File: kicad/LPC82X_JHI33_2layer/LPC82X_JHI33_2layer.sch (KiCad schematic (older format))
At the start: 27 parts, among them J1 Conn_02x09_Odd_Even, J2 Conn_02x09_Odd_Even, J3 JTAG_2X05, U1 LPC824M201JHI33, Y1 12MHz

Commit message: added bulk decoupling 0805 increased clearance of ground plane
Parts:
- added C7: 10u, SquantorRcl:C_0805, symbol Device:C
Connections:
- net VDD: now also C7.2
- net VSS: now also C7.1
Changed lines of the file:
@@
 EESchema Schematic File Version 4
-LIBS:LPC82X_JHI33-cache
 EELAYER 26 0
 EELAYER END
@@
 	1    0    0    -1
 $EndComp
+$Comp
+L Device:C C7
+U 1 1 5BD6A440
+P 2400 1700
+F 0 "C7" H 2515 1746 50  0000 L CNN
+F 1 "10u" H 2515 1655 50  0000 L CNN
+F 2 "SquantorRcl:C_0805" H 2438 1550 50  0001 C CNN
+F 3 "~" H 2400 1700 50  0001 C CNN
+	1    2400 1700
+	1    0    0    -1
+$EndComp
+$Comp
+L power:VSS #PWR0125
+U 1 1 5BD6A894
+P 2400 1500
+F 0 "#PWR0125" H 2400 1350 50  0001 C CNN
+F 1 "VSS" V 2417 1628 50  0000 L CNN
+F 2 "" H 2400 1500 50  0001 C CNN
+F 3 "" H 2400 1500 50  0001 C CNN
+	1    2400 1500
+	1    0    0    -1
+$EndComp
+$Comp
+L power:VDD #PWR0126
+U 1 1 5BD6A935
+P 2400 1900
+F 0 "#PWR0126" H 2400 1750 50  0001 C CNN
+F 1 "VDD" V 2417 2028 50  0000 L CNN
+F 2 "" H 2400 1900 50  0001 C CNN
+F 3 "" H 2400 1900 50  0001 C CNN
+	1    2400 1900
+	-1   0    0    1
+$EndComp
+Wire Wire Line
+	2400 1500 2400 1550
+Wire Wire Line
+	2400 1850 2400 1900
 $EndSCHEMATC

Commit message: silk screen updates
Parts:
- S1: value 2pin_tact_switch -> Reset
- S2: value 2pin_tact_switch -> Boot
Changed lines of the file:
@@
 EESchema Schematic File Version 4
+LIBS:LPC82X_JHI33_2layer-cache
 EELAYER 26 0
 EELAYER END
@@
 P 1850 4600
 F 0 "S1" H 1600 4700 60  0000 C CNN
-F 1 "2pin_tact_switch" H 1850 4831 60  0000 C CNN
+F 1 "Reset" H 1850 4831 60  0000 C CNN
 F 2 "SquantorButtons:TD-85XU" H 1850 4600 60  0001 C CNN
 F 3 "" H 1850 4600 60  0001 C CNN
@@
 P 1850 5100
 F 0 "S2" H 1600 5200 60  0000 C CNN
-F 1 "2pin_tact_switch" H 1850 5331 60  0000 C CNN
+F 1 "Boot" H 1850 5331 60  0000 C CNN
 F 2 "SquantorButtons:TD-85XU" H 1850 5100 60  0001 C CNN
 F 3 "" H 1850 5100 60  0001 C CNN

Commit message: updated versionnumber
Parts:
- N2: value 20181026 -> 20181028
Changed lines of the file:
@@
 P 850 7700
 F 0 "N2" H 850 7800 60  0000 C CNN
-F 1 "20181026" H 850 7700 60  0000 C CNN
+F 1 "20181028" H 850 7700 60  0000 C CNN
 F 2 "SquantorLabels:Label_version" H 850 7700 60  0001 C CNN
 F 3 "" H 850 7700 60  0001 C CNN

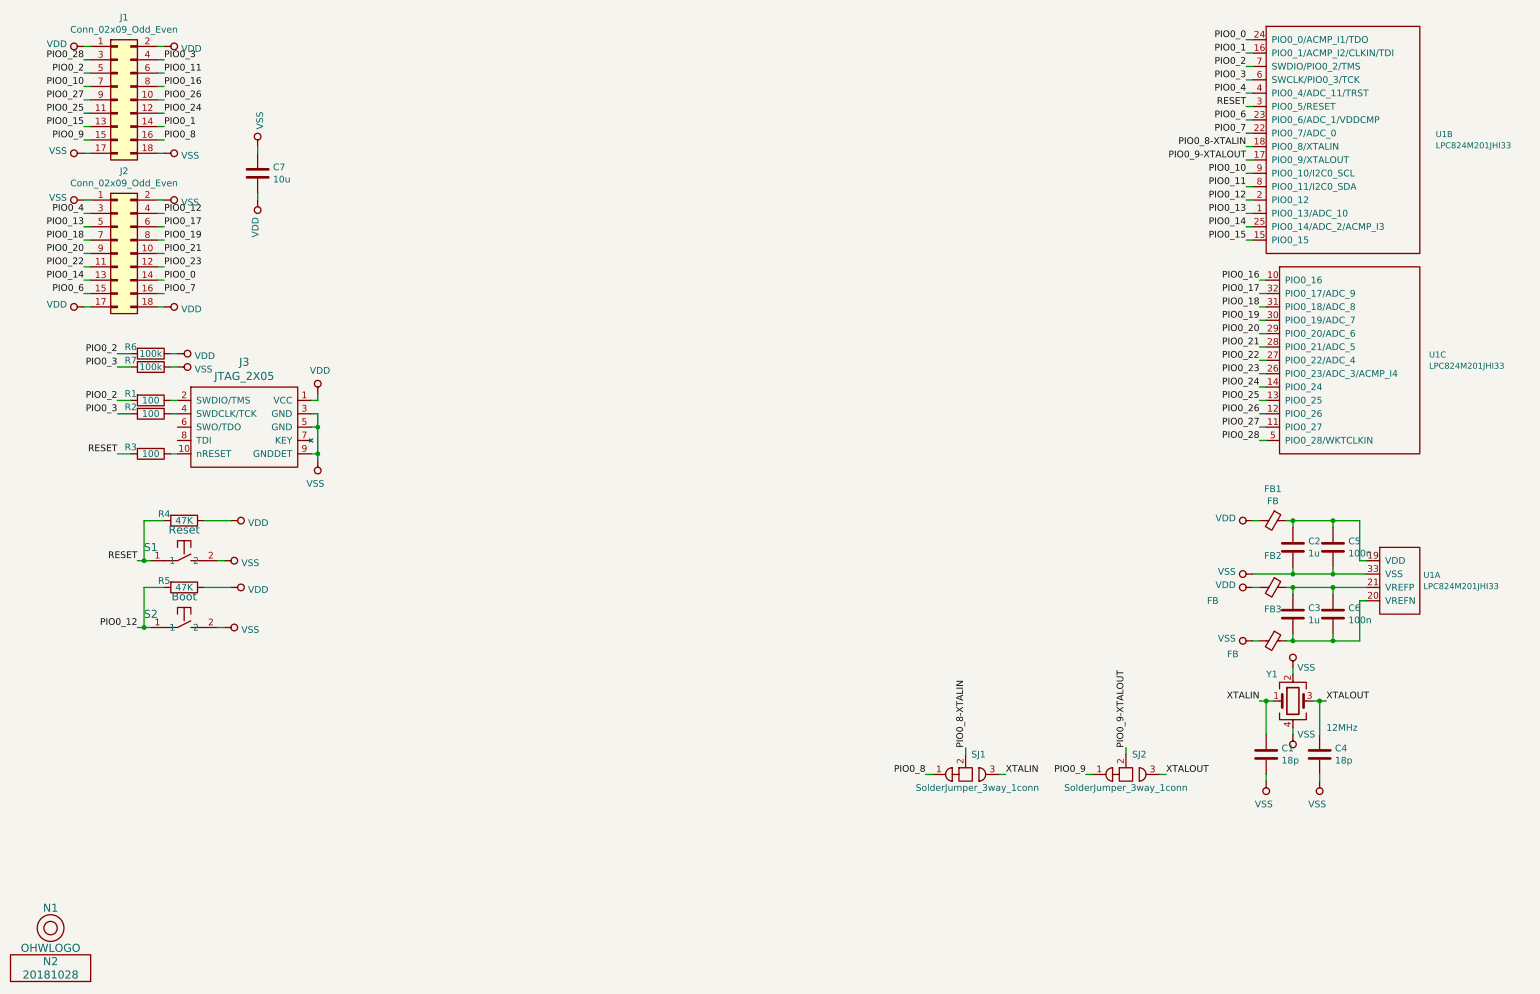
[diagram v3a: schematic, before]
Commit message: removed some parts from schematics to simplify the breakout
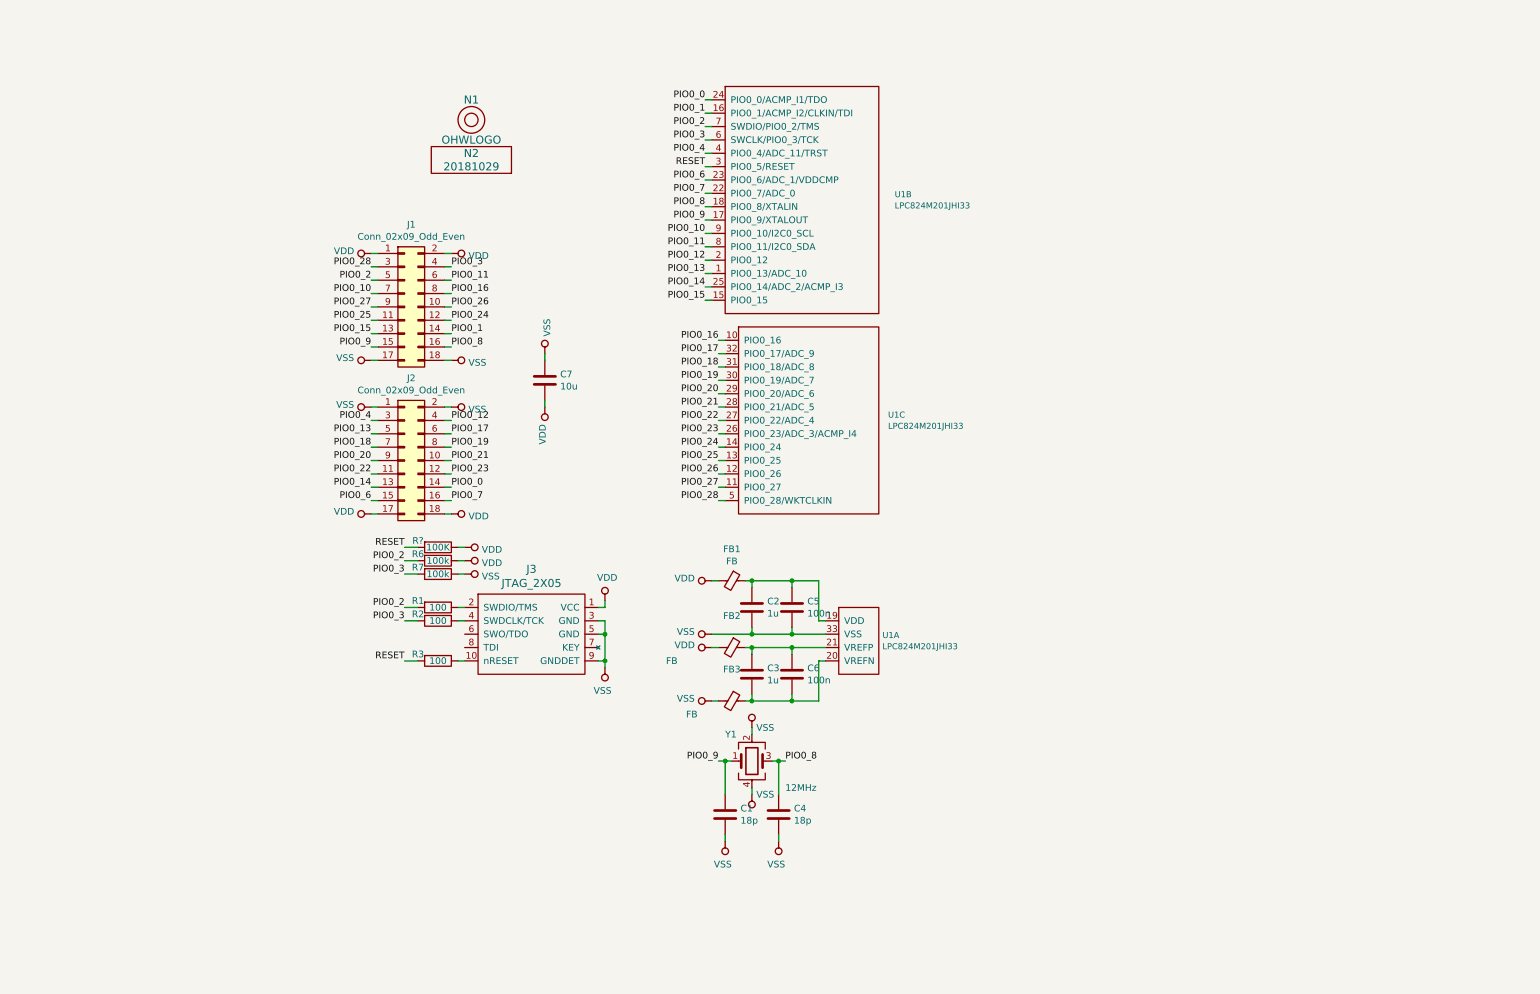
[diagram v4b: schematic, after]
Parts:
- removed R4, R5: 47K, SquantorRcl:R_0402_hand, symbol Device:R
- removed S1: Reset, SquantorButtons:TD-85XU, symbol SquantorButtons:2pin_tact_switch
- removed S2: Boot, SquantorButtons:TD-85XU, symbol SquantorButtons:2pin_tact_switch
- removed SJ1, SJ2: SolderJumper_3way_1conn, SquantorSpecial:solder_jumper_3way_12conn, symbol SquantorSpecial:SolderJumper_3way_1conn
- added R?: 100K, SquantorRcl:R_0402_hand, symbol Device:R
- N2: value 20181028 -> 20181029
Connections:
- net PIO0_8-XTALIN is gone; now on net PIO0_8: U1.18 (PIO0_8/XTALIN)
- net PIO0_9-XTALOUT is gone; now on net PIO0_9: U1.17 (PIO0_9/XTALOUT)
- net XTALIN is gone; now on net PIO0_9: C1.1, Y1.1
- net XTALOUT is gone; now on net PIO0_8: C4.1, Y1.3
- net RESET: now also R?.2
- net VDD: now also R?.1
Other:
- moved on the sheet: C1, C2, C3, C4, C5, C6, C7, FB1, FB2, FB3, J1, J2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

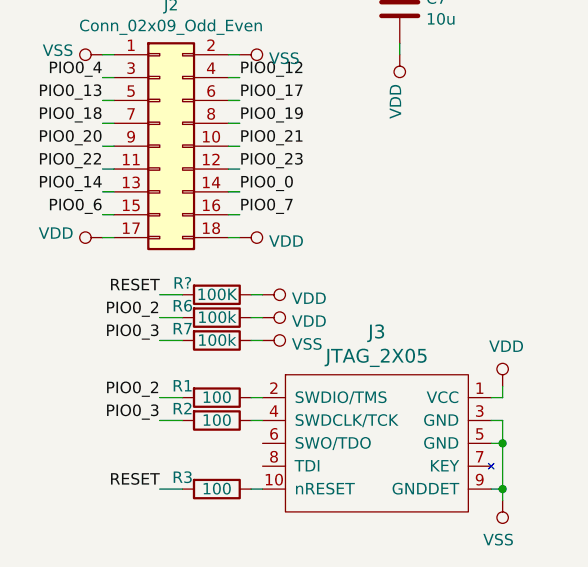
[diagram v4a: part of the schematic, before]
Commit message: updated schematic bits updated board and rerouted with some deletions, lets see if we can shrink the board a bit
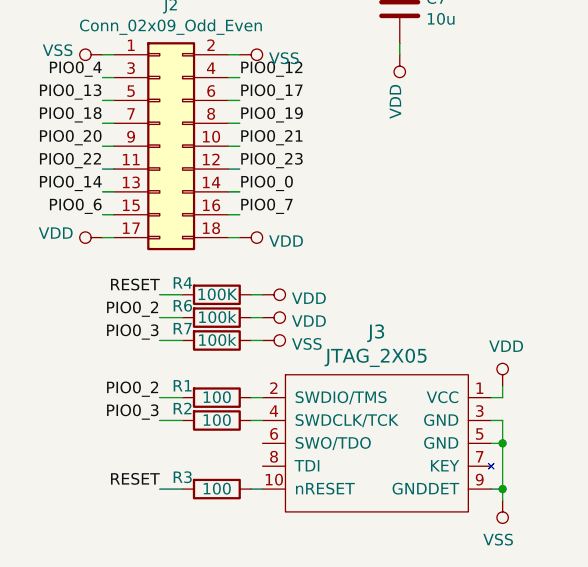
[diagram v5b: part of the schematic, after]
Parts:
- gave numbers to parts that had none: 1
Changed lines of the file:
@@
 PIO0_8
 $Comp
-L Device:R R?
+L Device:R R4
 U 1 1 5BD88002
 P 3750 4500
-F 0 "R?" V 3700 4350 50  0000 C CNN
+F 0 "R4" V 3700 4350 50  0000 C CNN
 F 1 "100K" V 3750 4500 50  0000 C CNN
 F 2 "SquantorRcl:R_0402_hand" V 3680 4500 50  0001 C CNN
@@
 RESET
 $Comp
-L power:VDD #PWR?
+L power:VDD #PWR0111
 U 1 1 5BD880D2
 P 3950 4500
-F 0 "#PWR?" H 3950 4350 50  0001 C CNN
+F 0 "#PWR0111" H 3950 4350 50  0001 C CNN
 F 1 "VDD" V 3967 4628 50  0000 L CNN
 F 2 "" H 3950 4500 50  0001 C CNN

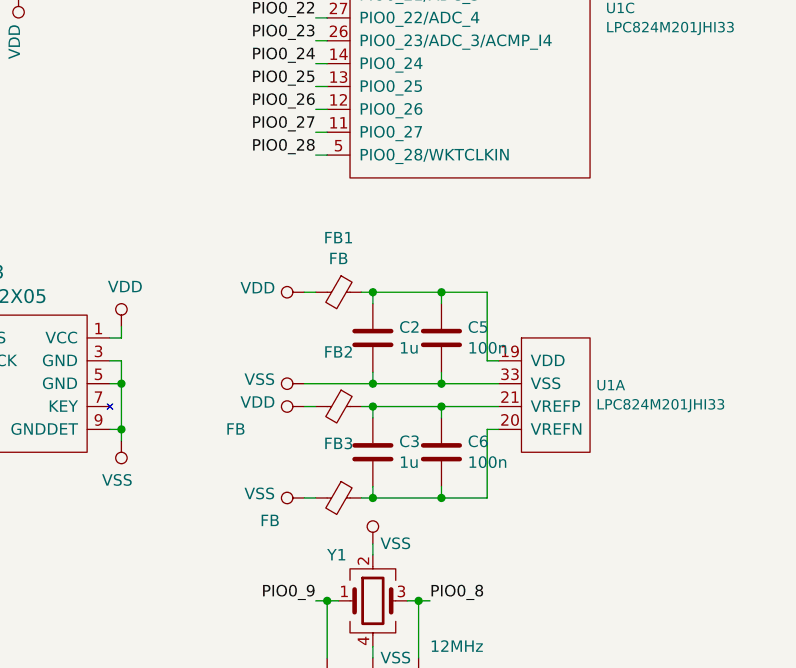
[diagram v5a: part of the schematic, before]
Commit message: updated schematic, added VDD jumper, added top groundplane, completed layout
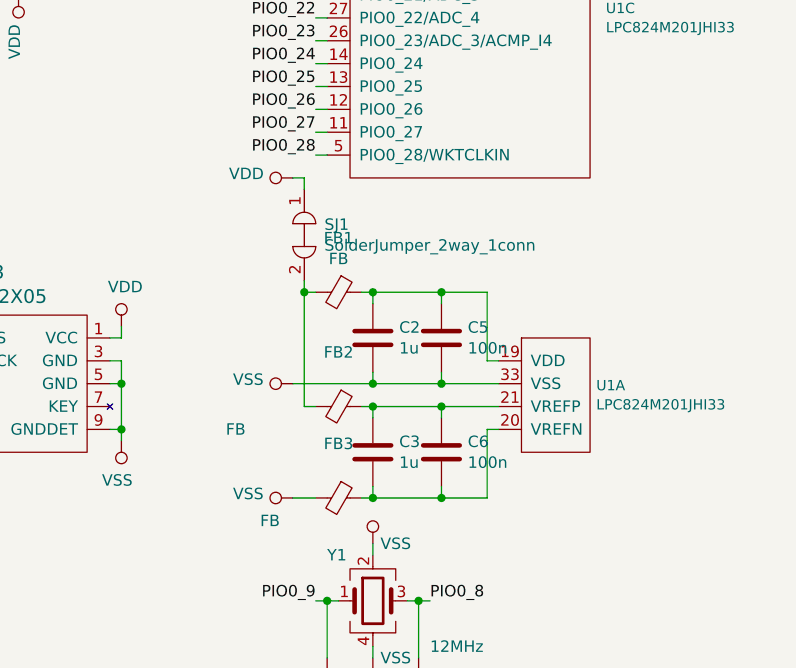
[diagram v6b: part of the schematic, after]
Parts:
- added SJ1: SolderJumper_2way_1conn, SquantorSpecial:solder_jumper_2way_conn, symbol SquantorSpecial:SolderJumper_2way_1conn
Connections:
- net VDD: now also SJ1.1; no longer FB1.2, FB2.2
- new net: FB1.2, FB2.2, SJ1.2
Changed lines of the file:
@@
 L power:VSS #PWR0101
 U 1 1 5BD2CC6A
-P 5800 5650
-F 0 "#PWR0101" H 5800 5500 50  0001 C CNN
-F 1 "VSS" V 5818 5778 50  0000 L CNN
-F 2 "" H 5800 5650 50  0001 C CNN
-F 3 "" H 5800 5650 50  0001 C CNN
-	1    5800 5650
-	0    -1   -1   0
-$EndComp
-$Comp
-L power:VDD #PWR0102
-U 1 1 5BD2CDC5
-P 5800 5250
-F 0 "#PWR0102" H 5800 5100 50  0001 C CNN
-F 1 "VDD" V 5818 5377 50  0000 L CNN
-F 2 "" H 5800 5250 50  0001 C CNN
-F 3 "" H 5800 5250 50  0001 C CNN
-	1    5800 5250
+P 5750 5650
+F 0 "#PWR0101" H 5750 5500 50  0001 C CNN
+F 1 "VSS" V 5768 5778 50  0000 L CNN
+F 2 "" H 5750 5650 50  0001 C CNN
+F 3 "" H 5750 5650 50  0001 C CNN
+	1    5750 5650
 	0    -1   -1   0
 $EndComp
@@
 L power:VSS #PWR0103
 U 1 1 5BD2CEDF
-P 5800 5150
-F 0 "#PWR0103" H 5800 5000 50  0001 C CNN
-F 1 "VSS" V 5818 5278 50  0000 L CNN
-F 2 "" H 5800 5150 50  0001 C CNN
-F 3 "" H 5800 5150 50  0001 C CNN
-	1    5800 5150
-	0    -1   -1   0
-$EndComp
-$Comp
-L power:VDD #PWR0104
-U 1 1 5BD2CF02
-P 5800 4750
-F 0 "#PWR0104" H 5800 4600 50  0001 C CNN
-F 1 "VDD" V 5818 4877 50  0000 L CNN
-F 2 "" H 5800 4750 50  0001 C CNN
-F 3 "" H 5800 4750 50  0001 C CNN
-	1    5800 4750
+P 5750 5150
+F 0 "#PWR0103" H 5750 5000 50  0001 C CNN
+F 1 "VSS" V 5768 5278 50  0000 L CNN
+F 2 "" H 5750 5150 50  0001 C CNN
+F 3 "" H 5750 5150 50  0001 C CNN
+	1    5750 5150
 	0    -1   -1   0
 $EndComp
@@
 Connection ~ 6100 5150
 Wire Wire Line
-	6100 5150 5800 5150
+	6100 5150 5750 5150
 Wire Wire Line
 	6400 5100 6400 5150
@@
 	5850 5250 5800 5250
 Wire Wire Line
-	5850 5650 5800 5650
+	5850 5650 5750 5650
 $Comp
 L Connector_Generic:Conn_02x09_Odd_Even J1
@@
 Wire Wire Line
 	3900 4500 3950 4500
+$Comp
+L power:VDD #PWR0102
+U 1 1 5BDA8246
+P 5750 4250
+F 0 "#PWR0102" H 5750 4100 50  0001 C CNN
+F 1 "VDD" V 5768 4377 50  0000 L CNN
+F 2 "" H 5750 4250 50  0001 C CNN
+F 3 "" H 5750 4250 50  0001 C CNN
+	1    5750 4250
+	0    -1   -1   0
+$EndComp
+Wire Wire Line
+	5800 5250 5800 4750
+Connection ~ 5800 4750
+Wire Wire Line
+	5800 4750 5800 4700
+$Comp
+L SquantorSpecial:SolderJumper_2way_1conn SJ1
+U 1 1 5BDC2411
+P 5800 4500
+F 0 "SJ1" V 5754 4588 50  0000 L CNN
+F 1 "SolderJumper_2way_1conn" V 5845 4588 50  0000 L CNN
+F 2 "SquantorSpecial:solder_jumper_2way_conn" H 5800 4500 50  0001 C CNN
+F 3 "" H 5800 4500 50  0001 C CNN
+	1    5800 4500
+	0    1    1    0
+$EndComp
+Wire Wire Line
+	5800 4300 5800 4250
+Wire Wire Line
+	5800 4250 5750 4250
 $EndSCHEMATC

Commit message: updated version number
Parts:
- N2: value 20181029 -> 20181102
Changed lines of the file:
@@
 P 4000 1650
 F 0 "N2" H 4000 1750 60  0000 C CNN
-F 1 "20181029" H 4000 1650 60  0000 C CNN
+F 1 "20181102" H 4000 1650 60  0000 C CNN
 F 2 "SquantorLabels:Label_version" H 4000 1650 60  0001 C CNN
 F 3 "" H 4000 1650 60  0001 C CNN

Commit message: updated version number
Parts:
- N2: value 20181102 -> 20181122
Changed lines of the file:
@@
 P 4000 1650
 F 0 "N2" H 4000 1750 60  0000 C CNN
-F 1 "20181102" H 4000 1650 60  0000 C CNN
+F 1 "20181122" H 4000 1650 60  0000 C CNN
 F 2 "SquantorLabels:Label_version" H 4000 1650 60  0001 C CNN
 F 3 "" H 4000 1650 60  0001 C CNN
